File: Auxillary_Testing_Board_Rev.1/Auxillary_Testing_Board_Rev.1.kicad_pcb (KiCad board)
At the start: 2 copper layers, 125.1 x 137.2 mm, 39 parts, among them SW1 SW_Push, SW10 SW_Push, SW11 SW_Push, SW12 SW_Push, SW13 SW_Push, SW14 SW_Push, SW15 SW_Push, SW16 SW_Push, SW17 SW_Push, SW18 SW_Push, SW19 SW_Push, SW2 SW_Push, SW20 SW_Push, SW21 SW_Push, SW22 SW_Push, SW23 SW_Push, SW24 SW_Push, SW25 SW_Push, SW26 SW_Push, SW27 SW_Push, SW28 SW_SPDT, SW3 SW_Push, SW4 SW_Push, SW5 SW_Push, SW6 SW_Push, SW7 SW_Push, SW8 SW_Push, SW9 SW_Push, U1 TM4C129E_Launchpad, U2 OKI

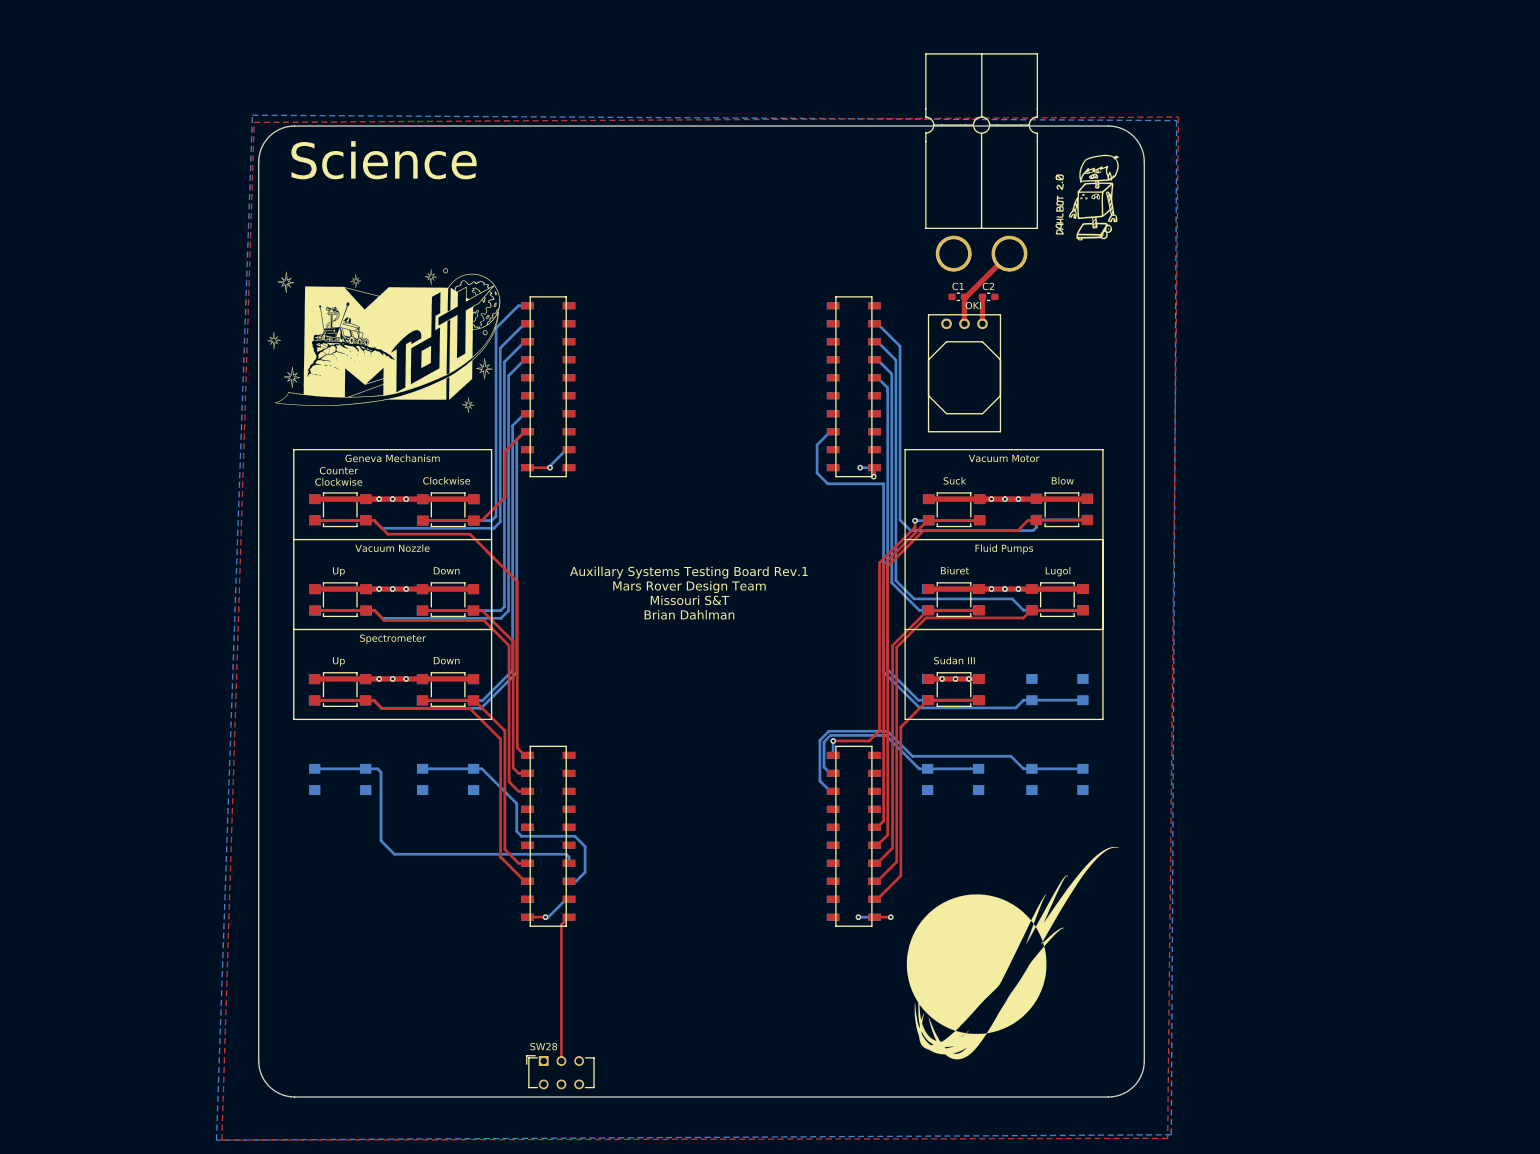
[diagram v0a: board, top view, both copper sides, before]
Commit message: Added LEDs to the schematic
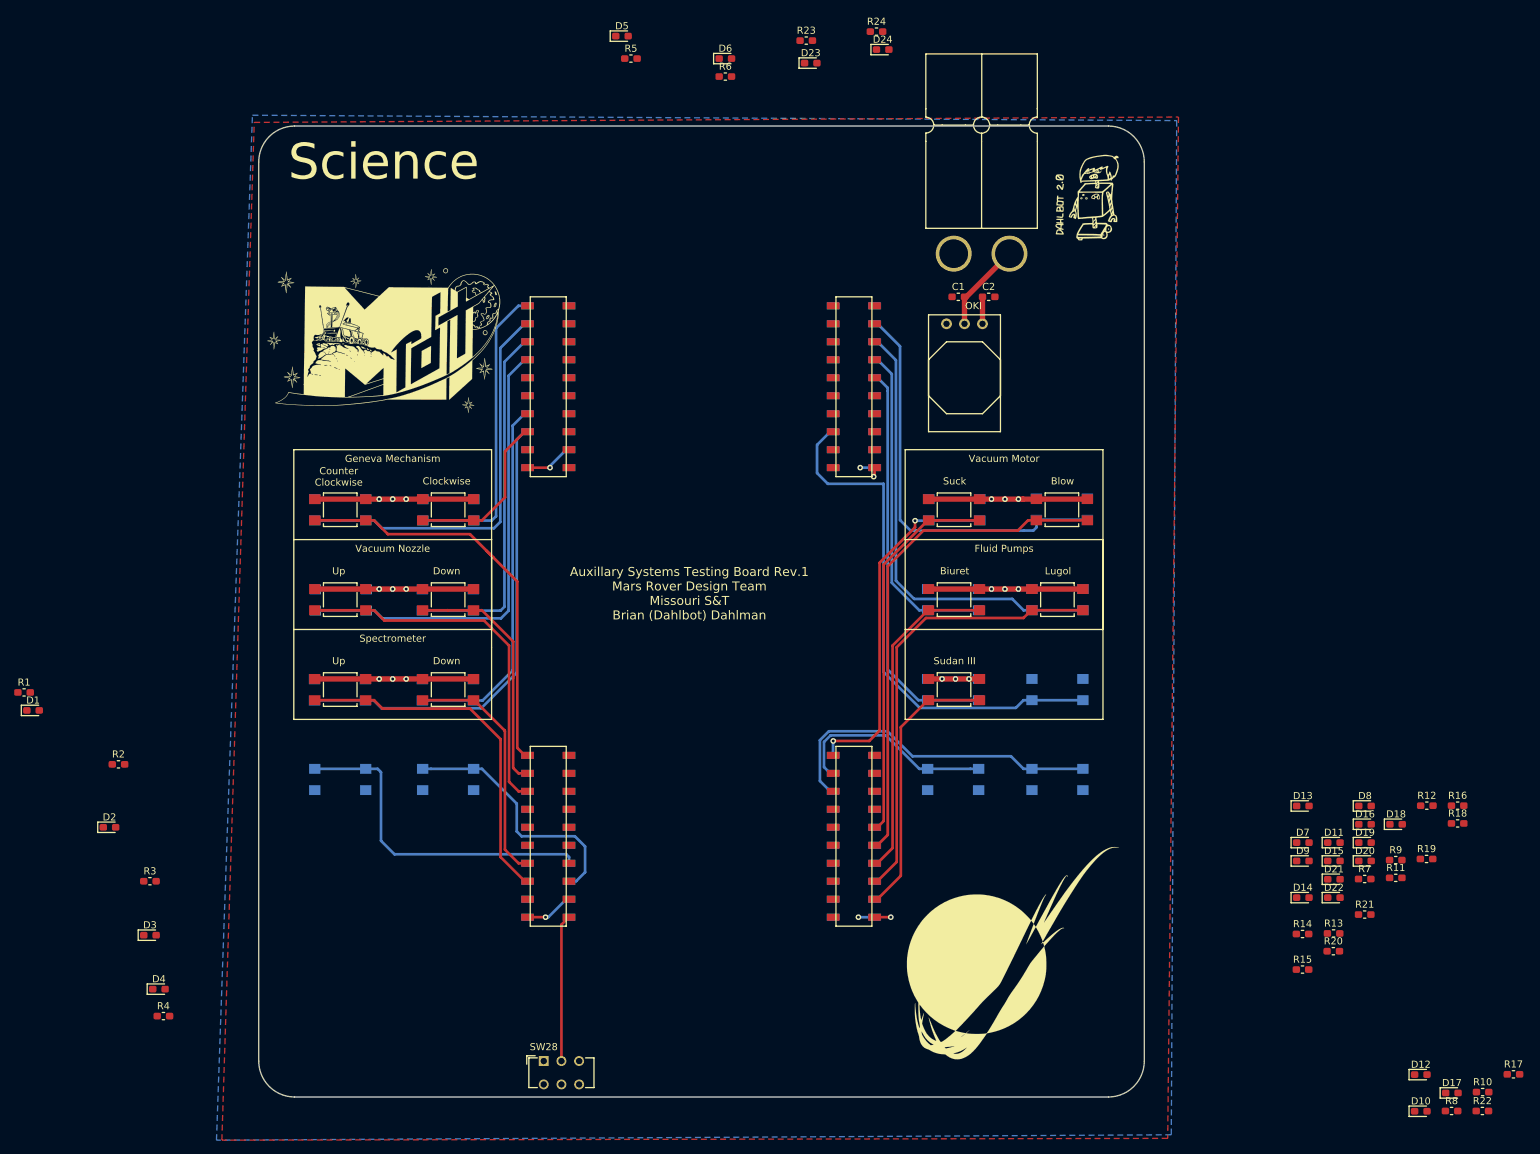
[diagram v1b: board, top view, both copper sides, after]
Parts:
- added D1: LED, LED_SMD:LED_0603_1608Metric_Pad1.05x0.95mm_HandSolder, F.Cu at (-16.5, 67.3)
- added D10: LED, LED_SMD:LED_0603_1608Metric_Pad1.05x0.95mm_HandSolder, F.Cu at (179.5, 123.9)
- added D11: LED, LED_SMD:LED_0603_1608Metric_Pad1.05x0.95mm_HandSolder, F.Cu at (167.2, 86.0)
- added D12: LED, LED_SMD:LED_0603_1608Metric_Pad1.05x0.95mm_HandSolder, F.Cu at (179.5, 118.8)
- added D13: LED, LED_SMD:LED_0603_1608Metric_Pad1.05x0.95mm_HandSolder, F.Cu at (162.9, 80.8)
- added D14: LED, LED_SMD:LED_0603_1608Metric_Pad1.05x0.95mm_HandSolder, F.Cu at (162.9, 93.8)
- added D15: LED, LED_SMD:LED_0603_1608Metric_Pad1.05x0.95mm_HandSolder, F.Cu at (167.2, 88.6)
- added D16: LED, LED_SMD:LED_0603_1608Metric_Pad1.05x0.95mm_HandSolder, F.Cu at (171.6, 83.4)
- added D17: LED, LED_SMD:LED_0603_1608Metric_Pad1.05x0.95mm_HandSolder, F.Cu at (183.9, 121.3)
- added D18: LED, LED_SMD:LED_0603_1608Metric_Pad1.05x0.95mm_HandSolder, F.Cu at (176.0, 83.4)
- added D19: LED, LED_SMD:LED_0603_1608Metric_Pad1.05x0.95mm_HandSolder, F.Cu at (171.6, 86.0)
- added D2: LED, LED_SMD:LED_0603_1608Metric_Pad1.05x0.95mm_HandSolder, F.Cu at (-5.71, 83.8)
- added D20: LED, LED_SMD:LED_0603_1608Metric_Pad1.05x0.95mm_HandSolder, F.Cu at (171.6, 88.6)
- added D21: LED, LED_SMD:LED_0603_1608Metric_Pad1.05x0.95mm_HandSolder, F.Cu at (167.2, 91.2)
- added D22: LED, LED_SMD:LED_0603_1608Metric_Pad1.05x0.95mm_HandSolder, F.Cu at (167.2, 93.8)
- added D23: LED, LED_SMD:LED_0603_1608Metric_Pad1.05x0.95mm_HandSolder, F.Cu at (93.3, -24.1)
- added D24: LED, LED_SMD:LED_0603_1608Metric_Pad1.05x0.95mm_HandSolder, F.Cu at (103.5, -26.0)
- added D3: LED, LED_SMD:LED_0603_1608Metric_Pad1.05x0.95mm_HandSolder, F.Cu at (0.00, 99.1)
- added D4: LED, LED_SMD:LED_0603_1608Metric_Pad1.05x0.95mm_HandSolder, F.Cu at (1.27, 106.7)
- added D5: LED, LED_SMD:LED_0603_1608Metric_Pad1.05x0.95mm_HandSolder, F.Cu at (66.7, -27.9)
- added D6: LED, LED_SMD:LED_0603_1608Metric_Pad1.05x0.95mm_HandSolder, F.Cu at (81.3, -24.8)
- added D7: LED, LED_SMD:LED_0603_1608Metric_Pad1.05x0.95mm_HandSolder, F.Cu at (162.9, 86.0)
- added D8: LED, LED_SMD:LED_0603_1608Metric_Pad1.05x0.95mm_HandSolder, F.Cu at (171.6, 80.8)
- added D9: LED, LED_SMD:LED_0603_1608Metric_Pad1.05x0.95mm_HandSolder, F.Cu at (162.9, 88.6)
- added R1: R, Resistor_SMD:R_0603_1608Metric_Pad1.05x0.95mm_HandSolder, F.Cu at (-17.8, 64.8)
- added R10: R, Resistor_SMD:R_0603_1608Metric_Pad1.05x0.95mm_HandSolder, F.Cu at (188.3, 121.2)
- added R11: R, Resistor_SMD:R_0603_1608Metric_Pad1.05x0.95mm_HandSolder, F.Cu at (176.0, 91.0)
- added R12: R, Resistor_SMD:R_0603_1608Metric_Pad1.05x0.95mm_HandSolder, F.Cu at (180.4, 80.8)
- added R13: R, Resistor_SMD:R_0603_1608Metric_Pad1.05x0.95mm_HandSolder, F.Cu at (167.2, 98.8)
- added R14: R, Resistor_SMD:R_0603_1608Metric_Pad1.05x0.95mm_HandSolder, F.Cu at (162.8, 98.9)
- added R15: R, Resistor_SMD:R_0603_1608Metric_Pad1.05x0.95mm_HandSolder, F.Cu at (162.8, 103.9)
- added R16: R, Resistor_SMD:R_0603_1608Metric_Pad1.05x0.95mm_HandSolder, F.Cu at (184.7, 80.8)
- added R17: R, Resistor_SMD:R_0603_1608Metric_Pad1.05x0.95mm_HandSolder, F.Cu at (192.6, 118.7)
- added R18: R, Resistor_SMD:R_0603_1608Metric_Pad1.05x0.95mm_HandSolder, F.Cu at (184.7, 83.3)
- added R19: R, Resistor_SMD:R_0603_1608Metric_Pad1.05x0.95mm_HandSolder, F.Cu at (180.3, 88.3)
- added R2: R, Resistor_SMD:R_0603_1608Metric_Pad1.05x0.95mm_HandSolder, F.Cu at (-4.45, 74.9)
- added R20: R, Resistor_SMD:R_0603_1608Metric_Pad1.05x0.95mm_HandSolder, F.Cu at (167.2, 101.3)
- added R21: R, Resistor_SMD:R_0603_1608Metric_Pad1.05x0.95mm_HandSolder, F.Cu at (171.6, 96.1)
- added R22: R, Resistor_SMD:R_0603_1608Metric_Pad1.05x0.95mm_HandSolder, F.Cu at (188.2, 123.9)
- added R23: R, Resistor_SMD:R_0603_1608Metric_Pad1.05x0.95mm_HandSolder, F.Cu at (92.7, -27.3)
- added R24: R, Resistor_SMD:R_0603_1608Metric_Pad1.05x0.95mm_HandSolder, F.Cu at (102.6, -28.6)
- added R3: R, Resistor_SMD:R_0603_1608Metric_Pad1.05x0.95mm_HandSolder, F.Cu at (0.00, 91.4)
- added R4: R, Resistor_SMD:R_0603_1608Metric_Pad1.05x0.95mm_HandSolder, F.Cu at (1.91, 110.5)
- added R5: R, Resistor_SMD:R_0603_1608Metric_Pad1.05x0.95mm_HandSolder, F.Cu at (67.9, -24.8)
- added R6: R, Resistor_SMD:R_0603_1608Metric_Pad1.05x0.95mm_HandSolder, F.Cu at (81.3, -22.2)
- added R7: R, Resistor_SMD:R_0603_1608Metric_Pad1.05x0.95mm_HandSolder, F.Cu at (171.6, 91.1)
- added R8: R, Resistor_SMD:R_0603_1608Metric_Pad1.05x0.95mm_HandSolder, F.Cu at (183.9, 123.9)
- added R9: R, Resistor_SMD:R_0603_1608Metric_Pad1.05x0.95mm_HandSolder, F.Cu at (176.0, 88.5)
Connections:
- C1 pad 1: GND -> Net-(C1-Pad1)
- C2 pad 2: GND -> Net-(C1-Pad2)
- Conn1 pad 2: GND -> (no net)
- U1 pad +3V3': +3V3 -> (no net)
- U1 pad PD0: Net-(U1-PadPD0) -> Spectrometer_Down_Ind
- U1 pad PD1: Net-(U1-PadPD1) -> Spectrometer_Up_Ind
- U1 pad PE0: Forearm_Clockwise -> Net-(U1-PadPE0)
- U1 pad PE1: Forearm_Counter_Clockwise -> Net-(U1-PadPE1)
- U1 pad PE3: Net-(U1-PadPE3) -> Connection_Ind
- U1 pad PF1: Mode_Toggle -> Net-(U1-PadPF1)
- U1 pad PK5: Gripper_Open -> Net-(U1-PadPK5)
- U1 pad PL1: Wrist_Counter_Clock -> Net-(U1-PadPL1)
- U1 pad PL2: Wrist_Clock -> Net-(U1-PadPL2)
- U1 pad PL3: Laser -> Net-(U1-PadPL3)
- U1 pad PL4: Net-(U1-PadPL4) -> Nozzle_Down_Ind
- U1 pad PL5: Net-(U1-PadPL5) -> Nozzle_Up_Ind
- U1 pad PN4: Base_Down -> Net-(U1-PadPN4)
- U1 pad PN5: Base_Up -> Net-(U1-PadPN5)
- U1 pad PP0: Base_Left -> Net-(U1-PadPP0)
- U1 pad PP1: Base_Right -> Net-(U1-PadPP1)
- U1 pad PP3: Wrist_Down -> Net-(U1-PadPP3)
- U1 pad PP4: Elbow_Down -> Net-(U1-PadPP4)
- U1 pad PQ0: Elbow_Up -> Net-(U1-PadPQ0)
- U1 pad PQ1: Solenoid -> Net-(U1-PadPQ1)
- U1 pad PQ2: Gripper_Close -> Net-(U1-PadPQ2)
- U1 pad PQ3: Wrist_Up -> Net-(U1-PadPQ3)
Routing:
- net (no net): track 0.00 -> 1.32 mm, vias 0 -> 1
- net +3V3: track 126.2 -> 124.9 mm, vias 20 -> 19
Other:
- board text added: "Auxillary Systems Testing Board Rev.1 Mars Rover Design Team Missouri S&T Brian (Dahlbot) Dahlman"
- board text removed: "Auxillary Systems Testing Board Rev.1 Mars Rover Design Team Missouri S&T Brian Dahlman"

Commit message: layout routed, just need to make it look good
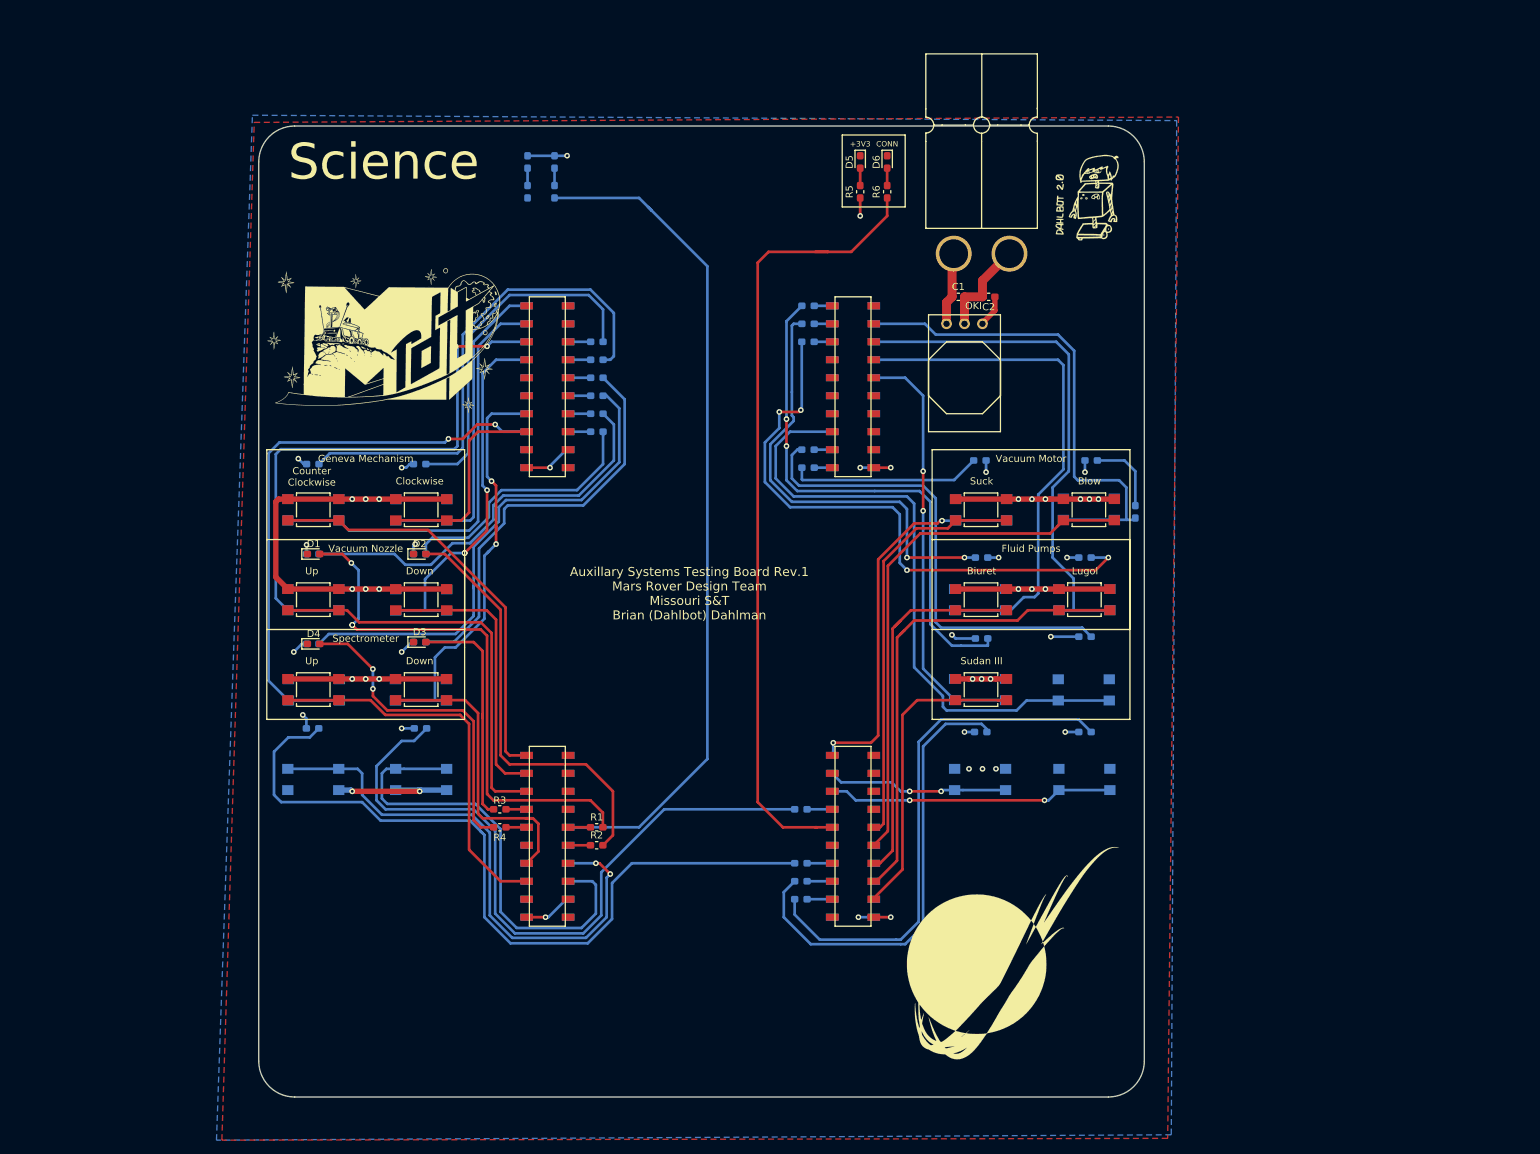
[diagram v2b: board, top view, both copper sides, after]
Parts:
- removed SW28: SW_SPDT, Button_Switch_THT:SW_CuK_JS202011AQN_DPDT_Angled
- D10, D11, D12, D13, D14, D15, D16, D17, D18, D19, D20, D21, D22, D23, D24, D7, D8, D9, R10, R11, R12, R13, R14, R15, R16, R17, R18, R19, R20, R21, R22, R23, R24, R7, R8, R9: moved to B.Cu
- moved R22 165.7 mm to (63.1, 15.2)
- moved D17 164.5 mm to (38.1, 45.2)
- moved R17 158.1 mm to (63.1, 27.9)
- moved D18 157.7 mm to (23.0, 45.2)
- moved D21 155.7 mm to (23.0, 32.5)
- moved D19 151.3 mm to (23.0, 57.9)
- moved R10 144.4 mm to (93.0, 12.7), turned to 180 degrees
- moved D22 142.9 mm to (38.1, 32.5)
- moved D14 141.9 mm to (23.0, 69.8)
- moved D20 137.1 mm to (38.1, 57.7)
- moved R18 134.7 mm to (63.1, 25.4)
- moved R19 134.2 mm to (63.1, 22.9)
- moved R21 133.8 mm to (63.1, 17.8)
- moved R20 131.8 mm to (63.1, 20.3)
- moved R8 128.5 mm to (93.0, 33.0), turned to 180 degrees
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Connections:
- C1 pad 2: Net-(C1-Pad2) -> GND
- C2 pad 2: Net-(C1-Pad2) -> GND
- Conn1 pad 1: Net-(C1-Pad2) -> GND
- Conn1 pad 2: (no net) -> Net-(C1-Pad1)
- R12 pad 1: Solenoid_Ind -> Solenoid
- U1 pad +3V3': (no net) -> +3V3
- U1 pad PB4: Net-(U1-PadPB4) -> Base_Left_Ind
- U1 pad PB5: Net-(U1-PadPB5) -> Base_Right_Ind
- U1 pad PE0: Net-(U1-PadPE0) -> Forearm_Clockwise
- U1 pad PE1: Net-(U1-PadPE1) -> Forearm_Counter_Clockwise
- U1 pad PF2: Net-(U1-PadPF2) -> Gripper_Open_Ind
- U1 pad PF3: Net-(U1-PadPF3) -> Gripper_Close_Ind
- U1 pad PG0: Net-(U1-PadPG0) -> Forearm_Counter_Clockwise_Ind
- U1 pad PG1: Net-(U1-PadPG1) -> Laser_Ind
- U1 pad PH1: Net-(U1-PadPH1) -> Wrist_Down_Ind
- U1 pad PK0: Net-(U1-PadPK0) -> Elbow_Up_Ind
- U1 pad PK1: Net-(U1-PadPK1) -> Elbow_Down_Ind
- U1 pad PK2: Net-(U1-PadPK2) -> Base_Up_Ind
- U1 pad PK3: Net-(U1-PadPK3) -> Base_Down_Ind
- U1 pad PK4: Net-(U1-PadPK4) -> Wrist_Counter_Clock_Ind
- U1 pad PK5: Net-(U1-PadPK5) -> Wrist_Counter_Clock
- U1 pad PK6: Net-(U1-PadPK6) -> Wrist_Up_Ind
- U1 pad PK7: Net-(U1-PadPK7) -> Wrist_Clock_Ind
- U1 pad PL0: Net-(U1-PadPL0) -> Forearm_Clockwise_Ind
- U1 pad PL1: Net-(U1-PadPL1) -> Gripper_Open
- U1 pad PL2: Net-(U1-PadPL2) -> Gripper_Close
- U1 pad PL3: Net-(U1-PadPL3) -> Laser
- U1 pad PN4: Net-(U1-PadPN4) -> Base_Down
- U1 pad PN5: Net-(U1-PadPN5) -> Base_Up
- U1 pad PP0: Net-(U1-PadPP0) -> Elbow_Up
- U1 pad PP1: Net-(U1-PadPP1) -> Elbow_Down
- U1 pad PP3: Net-(U1-PadPP3) -> Wrist_Down
- U1 pad PP4: Net-(U1-PadPP4) -> Base_Right
- U1 pad PQ0: Net-(U1-PadPQ0) -> Base_Left
- U1 pad PQ1: Net-(U1-PadPQ1) -> Solenoid
- U1 pad PQ2: Net-(U1-PadPQ2) -> Wrist_Clock
- U1 pad PQ3: Net-(U1-PadPQ3) -> Wrist_Up
- U2 pad 2: Net-(C1-Pad2) -> GND
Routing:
- net Connection_Ind: track 0.00 -> 233.2 mm
- net Net-(D14-Pad2): track 0.00 -> 110.8 mm
- net Net-(D13-Pad2): track 0.00 -> 98.6 mm
- net Net-(D11-Pad2): track 0.00 -> 84.5 mm, vias 0 -> 4
- net Net-(D1-Pad2): track 0.00 -> 76.1 mm, vias 0 -> 3
- net Net-(D9-Pad2): track 0.00 -> 75.3 mm, vias 0 -> 2
- net Net-(D16-Pad2): track 0.00 -> 74.0 mm
- net Net-(D19-Pad2): track 0.00 -> 70.9 mm
- net Net-(D21-Pad2): track 0.00 -> 70.4 mm
- net Net-(D7-Pad2): track 0.00 -> 66.8 mm
- net Net-(D15-Pad2): track 0.00 -> 64.5 mm
- net Net-(D10-Pad2): track 0.00 -> 62.7 mm, vias 0 -> 2
- net Net-(D2-Pad2): track 0.00 -> 60.6 mm
- net Net-(D20-Pad2): track 0.00 -> 58.6 mm
- net Net-(D18-Pad2): track 0.00 -> 56.8 mm
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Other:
- net class Default: trace_width 0.25 -> 0.381
- board text added: "+3V3"
- board text added: "Base"
- board text added: "CONN"
- board text added: "Wrist"
- board text removed: "Wrist Clockwise"
- board text removed: "Wrist Counter Clockwise"
